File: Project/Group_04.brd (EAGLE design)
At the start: 71.1 x 58.4 mm, 29 parts, among them J1 POWER_JACKPTH_LOCK, U1 +12v

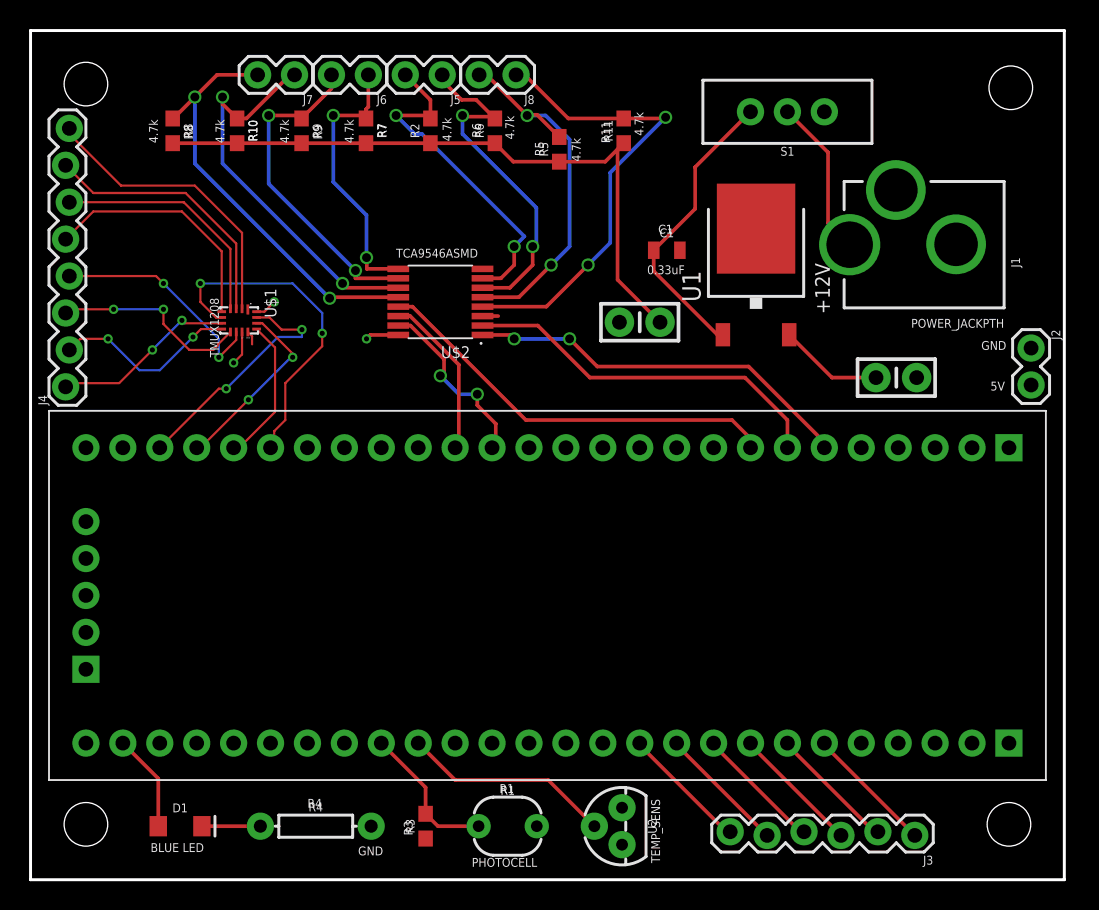
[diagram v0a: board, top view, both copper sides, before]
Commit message: warnings solved, some vias resized
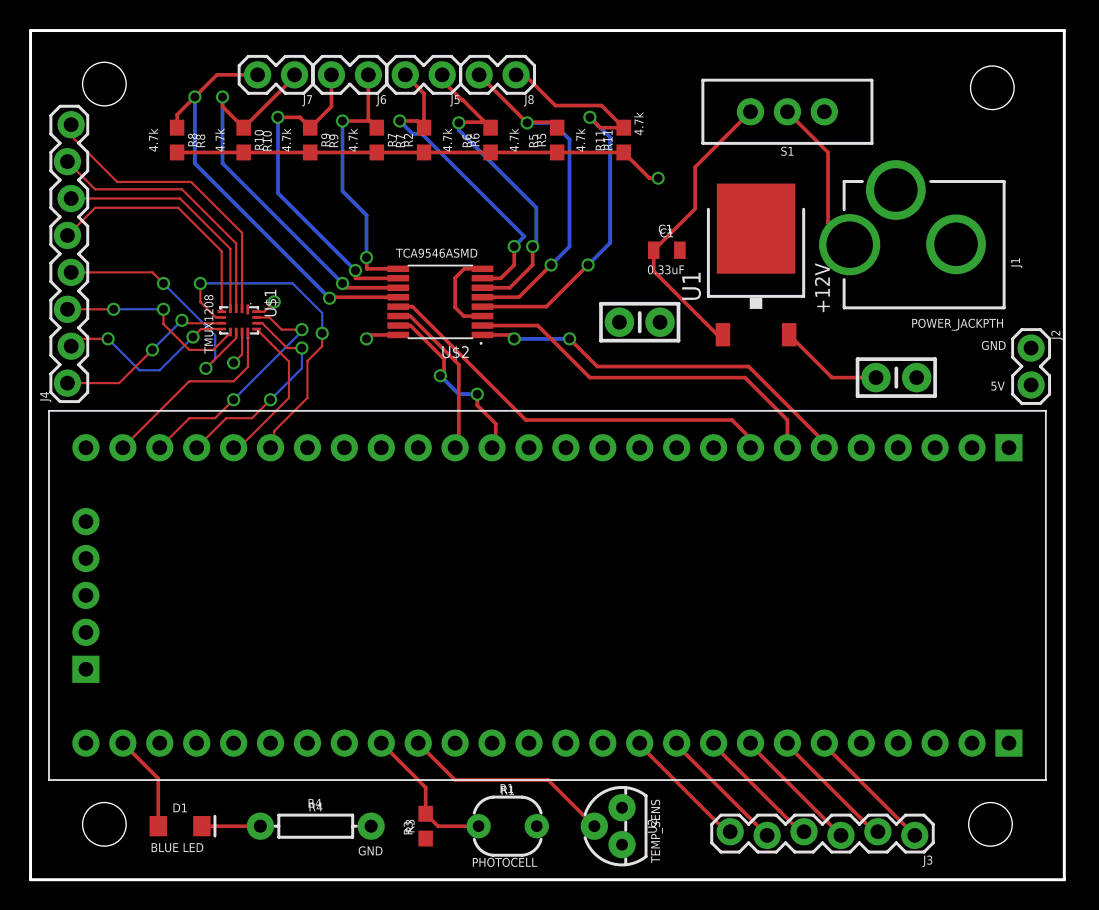
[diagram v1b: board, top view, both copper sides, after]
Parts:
- moved R7 0.98 mm to (23.8, 50.9)
- moved R9 0.87 mm to (19.2, 50.9)
- moved R10 0.78 mm to (14.7, 50.9)
- moved R2 0.77 mm to (27.1, 50.9)
- moved R8 0.70 mm to (10.1, 50.9)
- moved R6 0.70 mm to (31.6, 50.9)
- moved R5 0.65 mm to (36.2, 50.9)
- moved R11 0.64 mm to (40.8, 50.9)
- moved J4 0.28 mm to (2.67, 34.2)
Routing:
- net GND: track 2.05 -> 19.6 mm
- net 5V: track 59.2 -> 47.2 mm, vias 3 -> 4
- net N$5: track 15.6 -> 17.6 mm
- net MUX_A1: track 12.8 -> 14.7 mm
- net I2C_SDA_0: track 32.4 -> 31.4 mm
- net MUX_A2: track 10.1 -> 10.9 mm
- net I2C_SDA_3: track 27.5 -> 28.2 mm
- net I2C_SCL_0: track 25.7 -> 25.1 mm
- net I2C_SCL_1: track 23.3 -> 22.7 mm

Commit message: dimension fixed
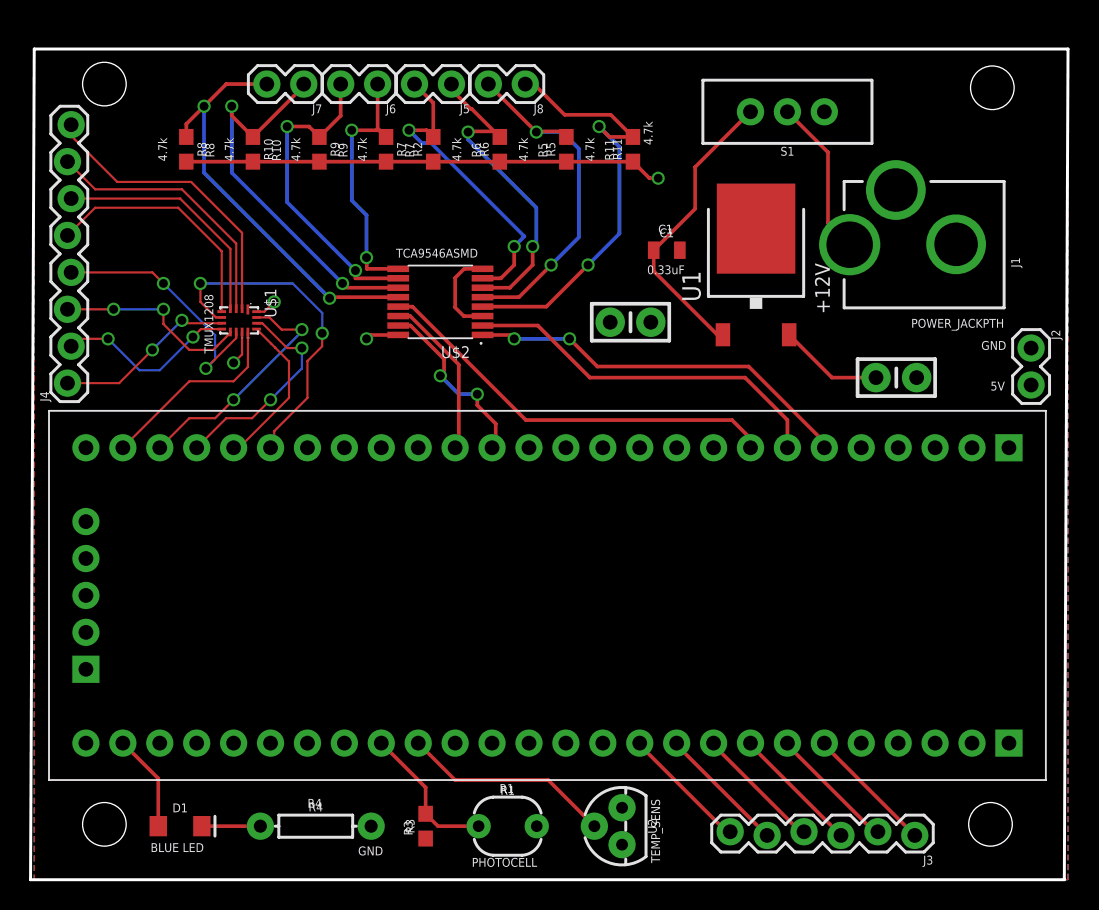
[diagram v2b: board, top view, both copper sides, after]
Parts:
- moved J6 0.90 mm to (23.9, 54.7)
- moved R6 0.90 mm to (32.3, 50.2)
- moved R9 0.90 mm to (19.9, 50.2)
- moved R10 0.90 mm to (15.3, 50.2)
- moved R8 0.90 mm to (10.7, 50.2)
- moved J5 0.90 mm to (29.0, 54.7)
- moved J7 0.90 mm to (18.8, 54.7)
- moved J8 0.90 mm to (34.0, 54.7)
- moved R11 0.90 mm to (41.4, 50.2)
- moved R2 0.90 mm to (27.7, 50.2)
- moved R5 0.90 mm to (36.9, 50.2)
- moved R7 0.90 mm to (24.5, 50.2)
- moved C2 0.63 mm to (41.3, 38.4)
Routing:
- net I2C_SCL_1: track 22.7 -> 21.8 mm
- net I2C_SDA_2: track 19.5 -> 18.6 mm
- net I2C_SCL_3: track 30.1 -> 29.2 mm
- net 5V: track 47.2 -> 46.3 mm
- net I2C_SDA_1: track 23.6 -> 22.7 mm
- net I2C_SCL_2: track 23.0 -> 22.1 mm
- net I2C_SDA_3: track 28.2 -> 27.3 mm
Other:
- board size 71.1 x 58.4 mm -> 71.4 x 57.1 mm
